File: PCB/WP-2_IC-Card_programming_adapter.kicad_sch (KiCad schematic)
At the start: 3 parts, among them J1 Conn_01x38_Male, J2 Conn_02x16_Counter_Clockwise, J3 Conn_02x08_Odd_Even

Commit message: local symbol & footprint library organization, add shielded mram version
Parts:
- J1: footprint 0_LOCAL:Pin_Header_Straight_1x38_Pitch1.27mm -> 000_LOCAL:Pin_Header_Straight_1x38_Pitch1.27mm; symbol 0_LOCAL:Conn_01x38_Male -> 000_LOCAL:Conn_01x38_Male
- J2: footprint 0_LOCAL:2x16x600 -> 000_LOCAL:2x16x600; symbol 0_LOCAL:Conn_02x16_Counter_Clockwise -> 000_LOCAL:Conn_02x16_Counter_Clockwise
- J3: footprint 0_LOCAL:2x8_jumper_block -> 000_LOCAL:2x8_jumper_block; symbol 0_LOCAL:Conn_02x08_Odd_Even -> 000_LOCAL:Conn_02x08_Odd_Even

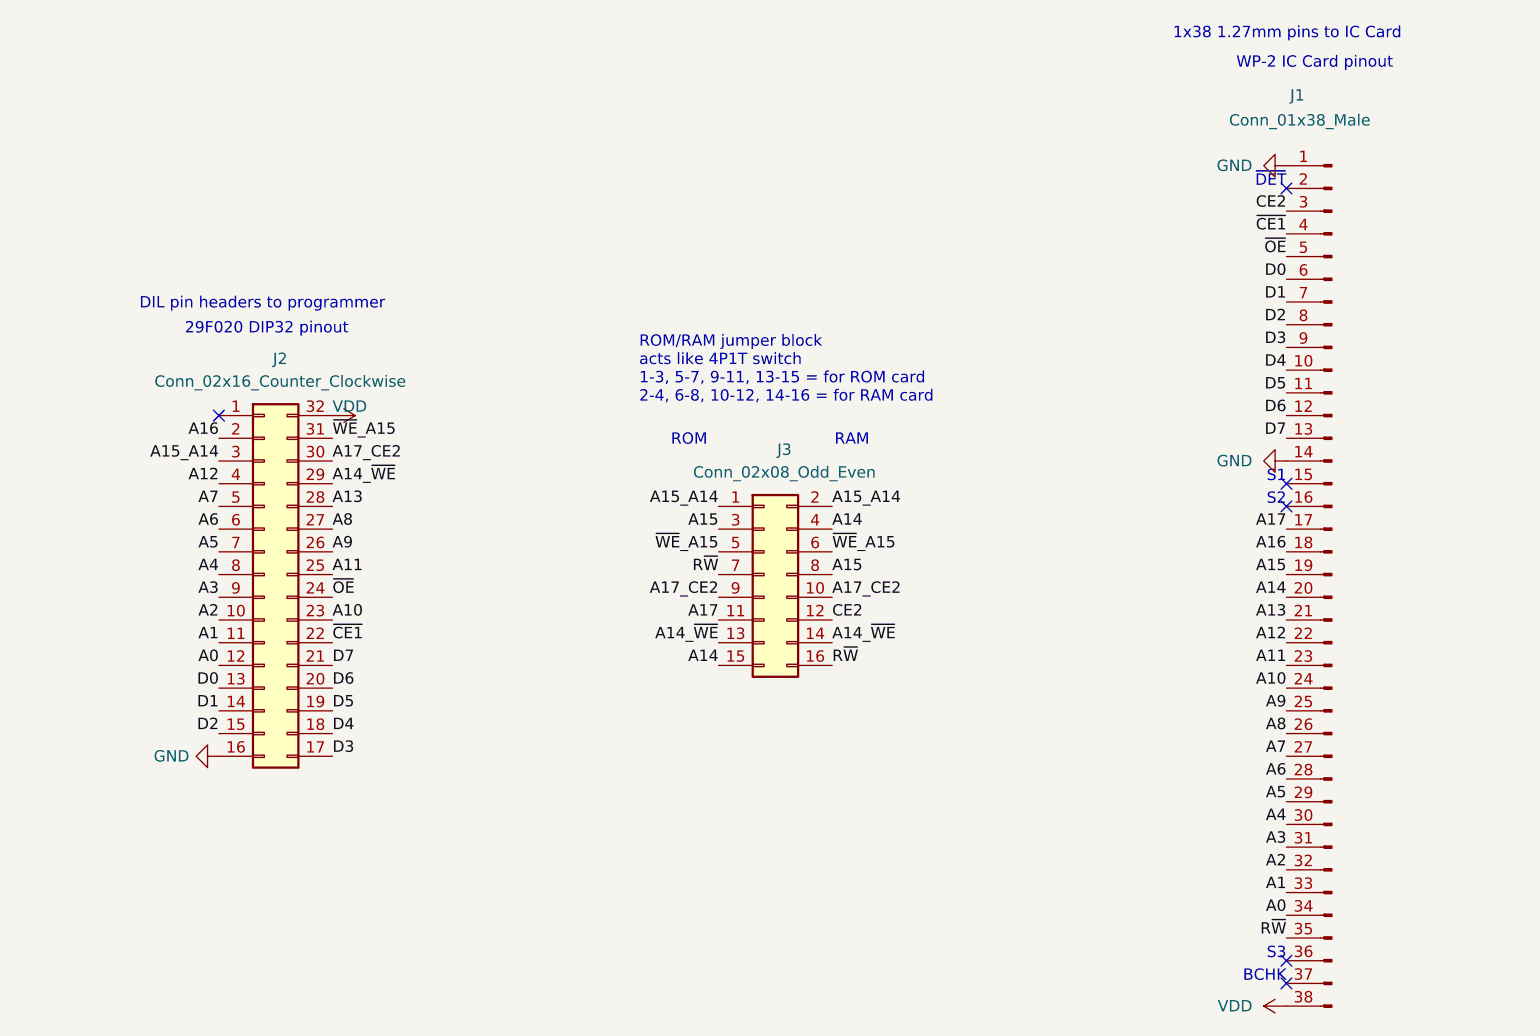
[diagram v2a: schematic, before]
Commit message: update programming adapter & readme
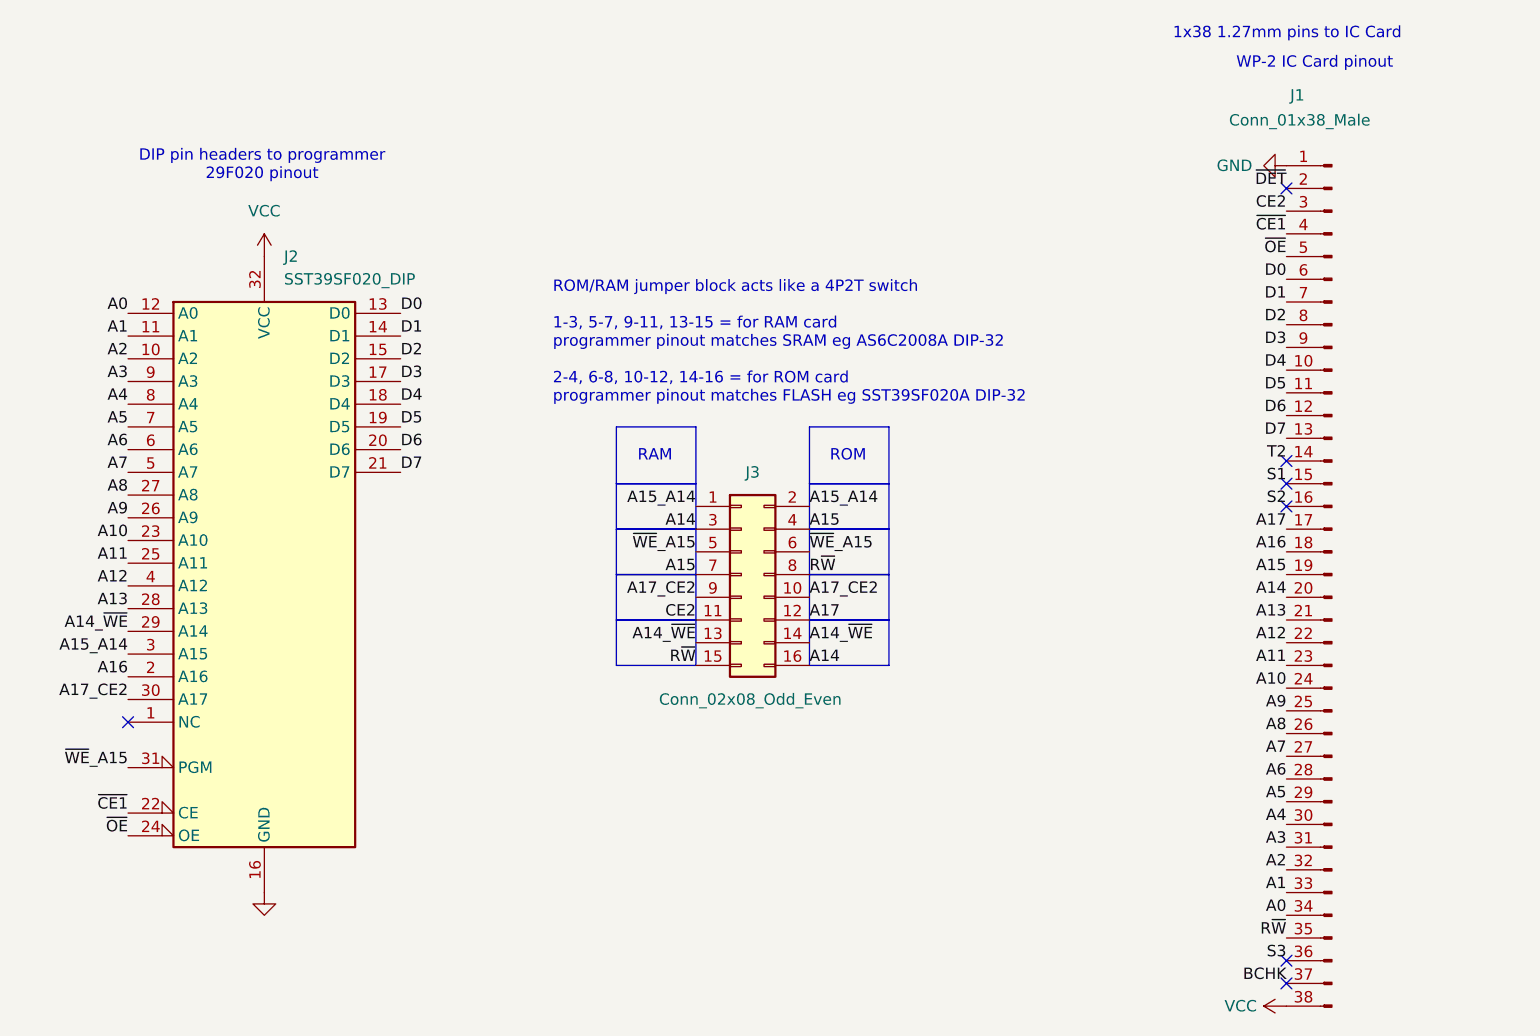
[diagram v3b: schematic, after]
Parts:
- removed J2: Conn_02x16_Counter_Clockwise, 000_LOCAL:2x16x600, symbol 000_LOCAL:Conn_02x16_Counter_Clockwise
- added J2: SST39SF020_DIP, 000_LOCAL:2x16x600, symbol 000_LOCAL:SST39SF020_DIP
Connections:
- net A0: now also J2.12 (A0)
- net A1: now also J2.11 (A1)
- net A10: now also J2.23 (A10)
- net A11: now also J2.25 (A11)
- net A12: now also J2.4 (A12)
- net A13: now also J2.28 (A13)
- net A14: now also J3.16 (Pin_16), J3.3 (Pin_3); no longer J3.15 (Pin_15), J3.4 (Pin_4)
- net A14_~{WE}: now also J2.29 (A14)
- net A15: now also J3.4 (Pin_4), J3.7 (Pin_7); no longer J3.3 (Pin_3), J3.8 (Pin_8)
- net A15_A14: now also J2.3 (A15)
- net A16: now also J2.2 (A16)
- net A17: now also J3.12 (Pin_12); no longer J3.11 (Pin_11)
- net A17_CE2: now also J2.30 (A17)
- net A2: now also J2.10 (A2)
- net A3: now also J2.9 (A3)
- net A4: now also J2.8 (A4)
- net A5: now also J2.7 (A5)
- net A6: now also J2.6 (A6)
- net A7: now also J2.5 (A7)
- net A8: now also J2.27 (A8)
- net A9: now also J2.26 (A9)
- net CE2: now also J3.11 (Pin_11); no longer J3.12 (Pin_12)
- net D0: now also J2.13 (D0)
- net D1: now also J2.14 (D1)
- net D2: now also J2.15 (D2)
- net D3: now also J2.17 (D3)
- net D4: now also J2.18 (D4)
- net D5: now also J2.19 (D5)
- net D6: now also J2.20 (D6)
- net D7: now also J2.21 (D7)
- net GND: now also J2.16 (GND); no longer J1.14 (Pin_14)
- net R~{W}: now also J3.15 (Pin_15), J3.8 (Pin_8); no longer J3.16 (Pin_16), J3.7 (Pin_7)
- net ~{CE1}: now also J2.22 (CE)
- net ~{OE}: now also J2.24 (OE)
- net ~{WE}_A15: now also J2.31 (PGM)
- net S1: now reaches J1.15 (Pin_15)
- net S2: now reaches J1.16 (Pin_16)
- net ~{DET}: now reaches J1.2 (Pin_2)
- net S3: now reaches J1.36 (Pin_36)
- net BCHK: now reaches J1.37 (Pin_37)
- net VDD renamed VCC
- net VCC: now also J2.32 (VCC)
- new net T2: J1.14 (Pin_14)
- no-connect marks 6 -> 7
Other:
- note added: "DIP pin headers to programmer 29F020 pinout"
- note added: "ROM/RAM jumper block acts like a 4P2T switch 1-3, 5-7, 9-11, 13-15 = for RAM card programmer pinout matches SRAM eg AS6C2008A DIP-32 2-4, 6-8, 10-12, 14-16 = for ROM card programmer pinout matches FLASH eg SST39SF020A DIP-32"
- note removed: "29F020 DIP32 pinout"
- note removed: "BCHK"
- note removed: "DIL pin headers to programmer"
- note removed: "ROM/RAM jumper block acts like 4P1T switch 1-3, 5-7, 9-11, 13-15 = for ROM card 2-4, 6-8, 10-12, 14-16 = for RAM card"
- note removed: "S1"
- note removed: "S2"
- note removed: "S3"
- note removed: "~{DET}"
- moved on the sheet: J3

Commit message: programming adapter traces away from pads
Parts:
- J1: footprint 000_LOCAL:Pin_Header_Straight_1x38_Pitch1.27mm -> 000_LOCAL:TMS-138-01-x-x_pcb_edge
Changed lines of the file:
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@@
 			)
 		)
-		(property "Footprint" "000_LOCAL:Pin_Header_Straight_1x38_Pitch1.27mm"
+		(property "Footprint" "000_LOCAL:TMS-138-01-x-x_pcb_edge"
 			(at 195.58 101.6 0)
 			(effects

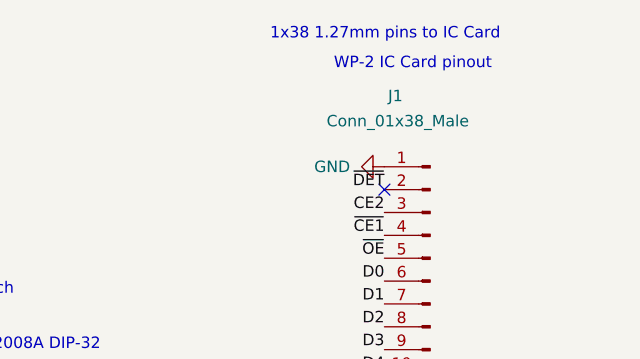
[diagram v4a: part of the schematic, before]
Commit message: add fancy programming adapters, horizontal tray, & full socket
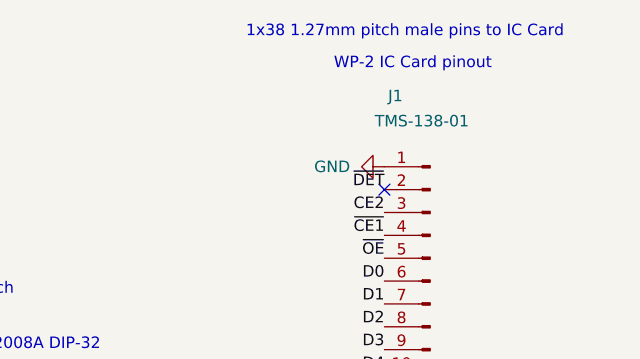
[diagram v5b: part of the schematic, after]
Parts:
- J1: value Conn_01x38_Male -> TMS-138-01; footprint 000_LOCAL:TMS-138-01-x-x_pcb_edge -> 000_LOCAL:TMS-138-01-x-x
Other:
- note added: "1x38 1.27mm pitch male pins to IC Card"
- note removed: "1x38 1.27mm pins to IC Card"
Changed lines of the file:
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@@
 		)
 	)
-	(text "1x38 1.27mm pins to IC Card"
+	(text "1x38 1.27mm pitch male pins to IC Card"
 		(exclude_from_sim no)
-		(at 177.8 41.91 0)
-		(effects
-			(font
-				(size 1.27 1.27)
-			)
-			(justify left bottom)
+		(at 192.786 41.656 0)
+		(effects
+			(font
+				(size 1.27 1.27)
+			)
+			(justify bottom)
 		)
 	)
@@
 			)
 		)
-		(property "Value" "Conn_01x38_Male"
+		(property "Value" "TMS-138-01"
 			(at 199.898 50.8 0)
 			(effects
@@
 			)
 		)
-		(property "Footprint" "000_LOCAL:TMS-138-01-x-x_pcb_edge"
+		(property "Footprint" "000_LOCAL:TMS-138-01-x-x"
 			(at 195.58 101.6 0)
 			(effects
